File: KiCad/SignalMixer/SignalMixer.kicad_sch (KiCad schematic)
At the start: 33 parts, among them SW1 SW_DIP_x08

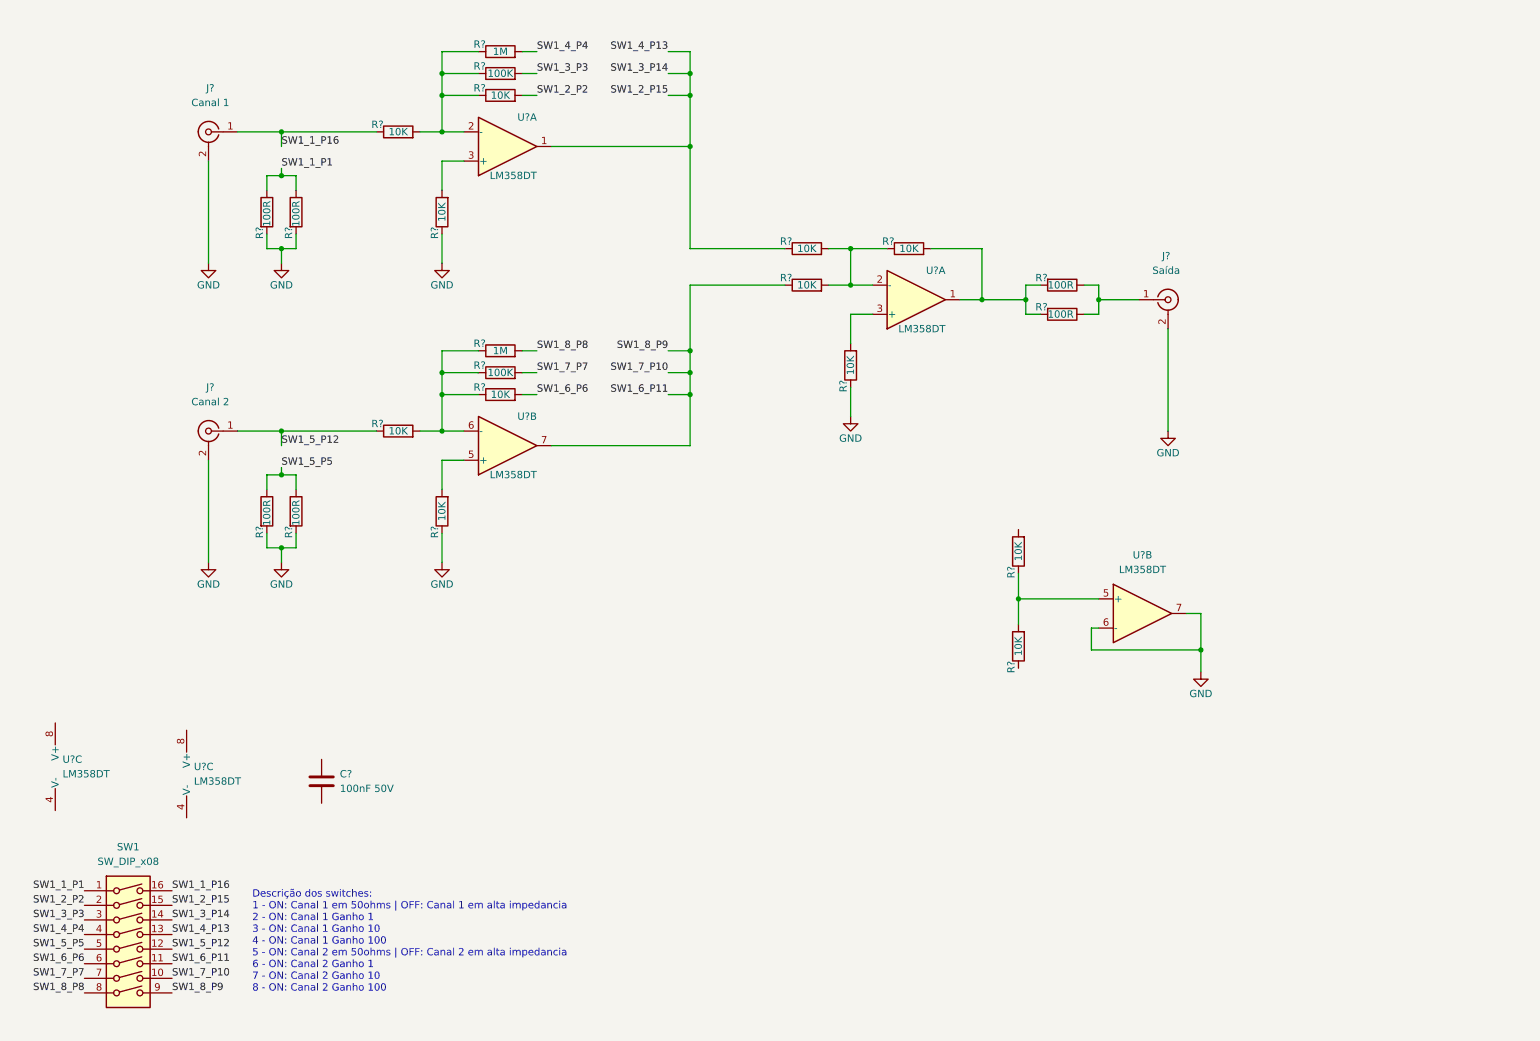
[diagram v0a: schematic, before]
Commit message: Finalização do diagrama esquematico e geração do diagrama em PDF.
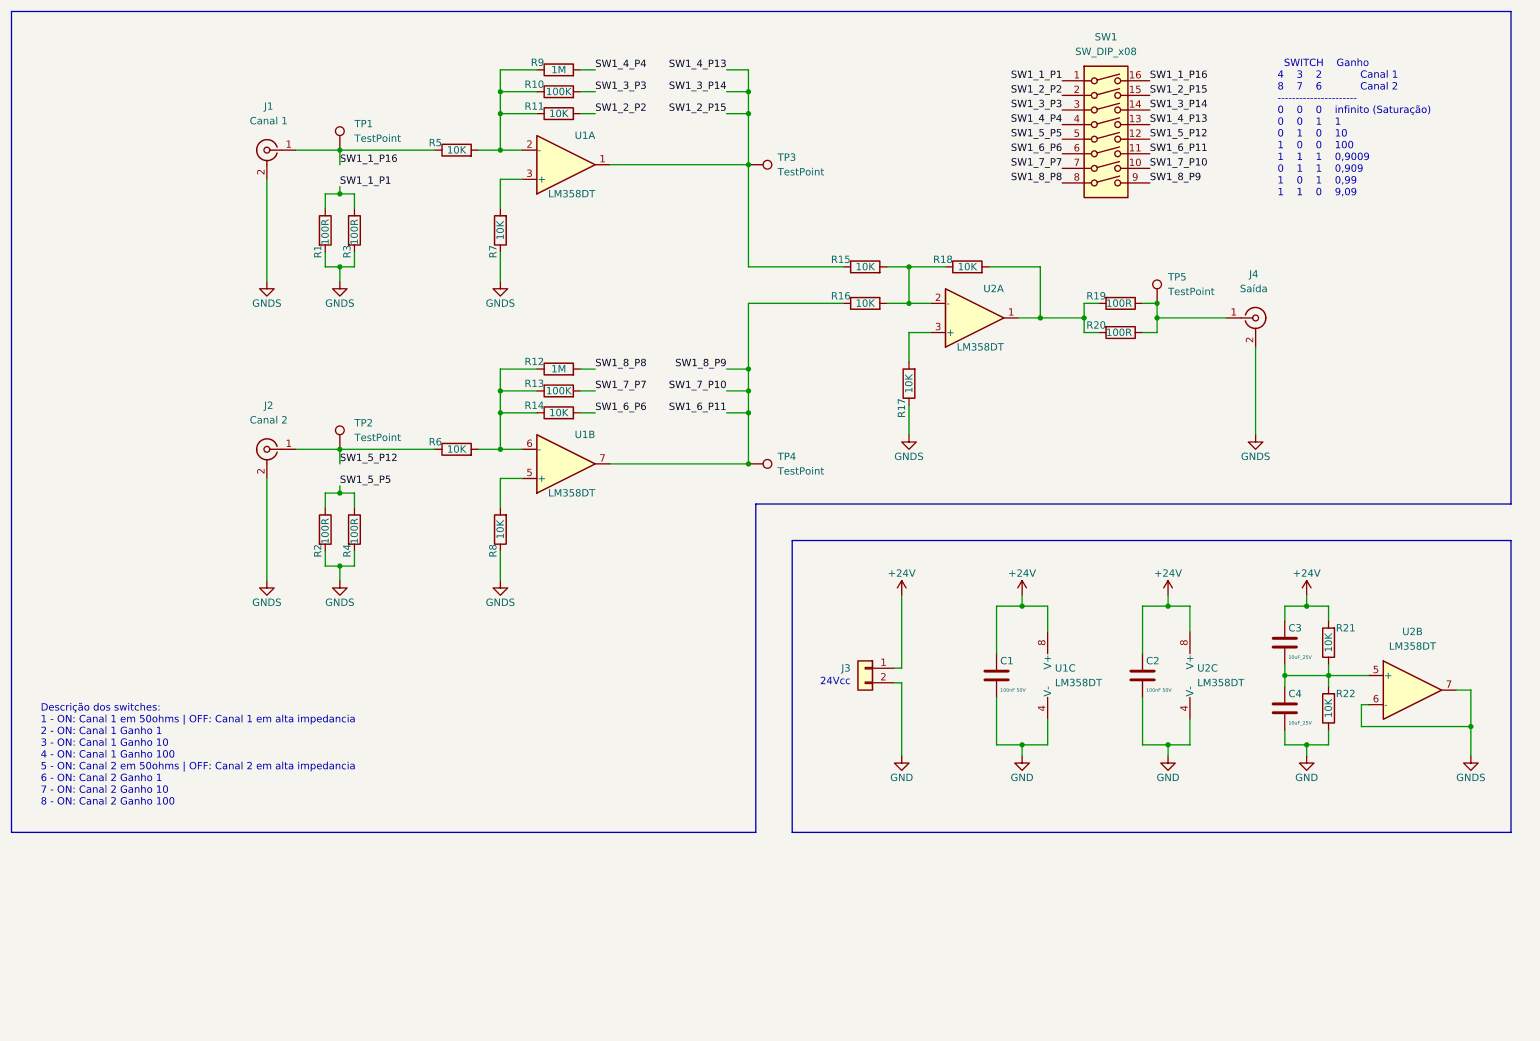
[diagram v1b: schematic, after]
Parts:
- added C1: 100nF 50V, Capacitor_SMD:C_0603_1608Metric, symbol Julio_Capacitores_0603:100nF 50V
- added C3, C4: 10uF_25V, Capacitor_SMD:C_0603_1608Metric, symbol Julio_Capacitores_0603:10uF_25V
- added J3: Conn_01x02, Julio_Connectors:JST_XH_B02B-XH-A_02x2.50mm_Straight, symbol Julio_Conectores:Conn_01x02
- added TP1, TP2, TP3, TP4, TP5: TestPoint, Julio_Testpoints:TestPoint_RH-5000, symbol Julio_Testpoint:TestPoint
- gave numbers to parts that had none: 28
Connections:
- net GND: now also C2.2, R22.1, U1.4 (V-), U2.4 (V-), C1.2, C4.2, J3.2 (Pin_2); no longer J1.2 (Ext), J2.2 (Ext), J4.2 (Ext), R1.2, R17.1, R2.2, R3.2, R4.2, R7.1, R8.1, U2.6 (-), U2.7
- net SW1_1_P16: now also TP1.1
- net SW1_2_P15: now also TP3.1
- net SW1_5_P12: now also TP2.1
- net SW1_6_P11: now also TP4.1
- net at R21.1, R22.2, U2.5 (+): now also C3.2, C4.1
- net +24V: now reaches U1.8 (V+)
- net +24V: now also C2.1, R21.2, U2.8 (V+), C1.1, C3.1, J3.1 (Pin_1)
- net at J4.1 (In), R19.1, R20.1: now also TP5.1
- new net GNDS: J1.2 (Ext), J2.2 (Ext), J4.2 (Ext), R1.2, R17.1, R2.2, R3.2, R4.2, R7.1, R8.1, U2.6 (-), U2.7
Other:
- note added: "24Vcc"
- note added: "SWITCH Ganho 4 3 2 Canal 1 8 7 6 Canal 2 ---------------------- 0 0 0 infinito (Saturação) 0 0 1 1 0 1 0 10 1 0 0 100 1 1 1 0,9009 0 1 1 0,909 1 0 1 0,99 1 1 0 9,09"
- moved on the sheet: C2, J1, J2, J4, R1, R10, R11, R12, R13, R14, R15, R16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

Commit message: Adicionado resistor de 1M nas entradas para evitar flutuacao quando o resistor de 50 ohms for desconectado.
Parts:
- added R1, R2: 1M, Resistor_SMD:R_0603_1608Metric, symbol Julio_Resistores_0603:1M
- added TP6: GNDS, Julio_Testpoints:TestPoint_RH-5000, symbol Julio_Testpoint:TestPoint
- TP1: value TestPoint -> Canal 1
- TP2: value TestPoint -> Canal 2
- TP3: value TestPoint -> Canal_1_G
- TP4: value TestPoint -> Canal_2_G
- TP5: value TestPoint -> Saída
- renumbered R8 to R10, R9 to R11, R10 to R12, R11 to R13, R12 to R14, R13 to R15, R14 to R16, R15 to R17, R16 to R18, R17 to R19, R18 to R20, R19 to R21, R20 to R22, R21 to R23, R22 to R24, R1 to R3, R2 to R4, R3 to R5, R4 to R6, R5 to R7, R6 to R8, R7 to R9
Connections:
- net GNDS: now also R1.1, R2.1, TP6.1
- net SW1_1_P16: now also R1.2
- net SW1_5_P12: now also R2.2
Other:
- moved on the sheet: J1, J2

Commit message: Definicao dos footprints, atualizacao do esquematico e inicio do roteamento da pcb.
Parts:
- J1, J2, J4: footprint (none) -> Julio_Connectors:BNC_DOSIN-801-0083
- SW1: footprint (none) -> Julio_Switches:SW_DIP_SPSTx08_Slide_9.78x22.5mm_W7.62mm_P2.54mm
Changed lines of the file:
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@@
     (property "Reference" "J2" (id 0) (at 59.3724 85.725 0))
     (property "Value" "Canal 2" (id 1) (at 59.3724 88.265 0))
-    (property "Footprint" "" (id 2) (at 59.055 93.345 0)
+    (property "Footprint" "Julio_Connectors:BNC_DOSIN-801-0083" (id 2) (at 59.055 93.345 0)
       (effects (font (size 1.27 1.27)) hide)
     )
@@
     (property "Reference" "J1" (id 0) (at 59.3724 33.655 0))
     (property "Value" "Canal 1" (id 1) (at 59.3724 36.195 0))
-    (property "Footprint" "" (id 2) (at 59.055 41.275 0)
+    (property "Footprint" "Julio_Connectors:BNC_DOSIN-801-0083" (id 2) (at 59.055 41.275 0)
       (effects (font (size 1.27 1.27)) hide)
     )
@@
     (property "Reference" "SW1" (id 0) (at 208.28 21.59 0))
     (property "Value" "SW_DIP_x08" (id 1) (at 208.28 24.13 0))
-    (property "Footprint" "" (id 2) (at 208.28 39.37 0)
+    (property "Footprint" "Julio_Switches:SW_DIP_SPSTx08_Slide_9.78x22.5mm_W7.62mm_P2.54mm" (id 2) (at 208.28 39.37 0)
       (effects (font (size 1.27 1.27)) hide)
     )
@@
     (property "Reference" "J4" (id 0) (at 233.9976 62.865 0))
     (property "Value" "Saída" (id 1) (at 233.9976 65.405 0))
-    (property "Footprint" "" (id 2) (at 234.315 70.485 0)
+    (property "Footprint" "Julio_Connectors:BNC_DOSIN-801-0083" (id 2) (at 234.315 70.485 0)
       (effects (font (size 1.27 1.27)) hide)
     )
@@
     )
     (path "/39b16d0f-89a0-4830-b92f-38d2db5dc07c"
-      (reference "J1") (unit 1) (value "Canal 1") (footprint "")
+      (reference "J1") (unit 1) (value "Canal 1") (footprint "Julio_Connectors:BNC_DOSIN-801-0083")
     )
     (path "/16ce34b0-e124-4278-9fc6-baaedcea88cf"
-      (reference "J2") (unit 1) (value "Canal 2") (footprint "")
+      (reference "J2") (unit 1) (value "Canal 2") (footprint "Julio_Connectors:BNC_DOSIN-801-0083")
     )
     (path "/bc0472ee-2a85-4c9e-9973-2a70e59d9a38"
@@
     )
     (path "/fd9f33df-4147-42df-b32c-afff44c62ea6"
-      (reference "J4") (unit 1) (value "Saída") (footprint "")
+      (reference "J4") (unit 1) (value "Saída") (footprint "Julio_Connectors:BNC_DOSIN-801-0083")
     )
     (path "/8aa91818-5460-4125-a3fc-f6a1805355d8"
@@
     )
     (path "/a2e06167-8355-4f4e-b078-7812a4ea3125"
-      (reference "SW1") (unit 1) (value "SW_DIP_x08") (footprint "")
+      (reference "SW1") (unit 1) (value "SW_DIP_x08") (footprint "Julio_Switches:SW_DIP_SPSTx08_Slide_9.78x22.5mm_W7.62mm_P2.54mm")
     )
     (path "/be7bc791-805c-4e3e-9832-26badc2c2d82"

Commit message: Finalizacao do layout da PCB.
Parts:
- added H1, H2, H3, H4: MountingHole, MountingHole:MountingHole_3.2mm_M3, symbol Mechanical:MountingHole
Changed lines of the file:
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@@
     (pin "2")
+  )
+  (symbol (lib_id "Mechanical:MountingHole") (at 153.035 180.34 0) (unit 1)
+    (in_bom no) (on_board yes) (fields_autoplaced)
+    (property "Reference" "H2" (id 0) (at 156.21 179.0699 0)
+      (effects (font (size 1.27 1.27)) (justify left))
+    )
+    (property "Value" "MountingHole" (id 1) (at 156.21 181.6099 0)
+      (effects (font (size 1.27 1.27)) (justify left))
+    )
+    (property "Footprint" "MountingHole:MountingHole_3.2mm_M3" (id 2) (at 153.035 180.34 0)
+      (effects (font (size 1.27 1.27)) hide)
+    )
+    (property "Datasheet" "~" (id 3) (at 153.035 180.34 0)
+      (effects (font (size 1.27 1.27)) hide)
+    )
   )
   (symbol (lib_id "Julio_Resistores_0603:1M") (at 66.675 107.315 180) (unit 1)
@@
     (pin "1")
     (pin "2")
+  )
+  (symbol (lib_id "Mechanical:MountingHole") (at 153.035 186.055 0) (unit 1)
+    (in_bom no) (on_board yes) (fields_autoplaced)
+    (property "Reference" "H3" (id 0) (at 156.21 184.7849 0)
+      (effects (font (size 1.27 1.27)) (justify left))
+    )
+    (property "Value" "MountingHole" (id 1) (at 156.21 187.3249 0)
+      (effects (font (size 1.27 1.27)) (justify left))
+    )
+    (property "Footprint" "MountingHole:MountingHole_3.2mm_M3" (id 2) (at 153.035 186.055 0)
+      (effects (font (size 1.27 1.27)) hide)
+    )
+    (property "Datasheet" "~" (id 3) (at 153.035 186.055 0)
+      (effects (font (size 1.27 1.27)) hide)
+    )
   )
   (symbol (lib_id "Julio_OpAmp:LM358DT") (at 261.62 135.255 0) (unit 2)
@@
     (pin "2")
   )
+  (symbol (lib_id "Mechanical:MountingHole") (at 153.035 191.77 0) (unit 1)
+    (in_bom no) (on_board yes) (fields_autoplaced)
+    (property "Reference" "H4" (id 0) (at 156.21 190.4999 0)
+      (effects (font (size 1.27 1.27)) (justify left))
+    )
+    (property "Value" "MountingHole" (id 1) (at 156.21 193.0399 0)
+      (effects (font (size 1.27 1.27)) (justify left))
+    )
+    (property "Footprint" "MountingHole:MountingHole_3.2mm_M3" (id 2) (at 153.035 191.77 0)
+      (effects (font (size 1.27 1.27)) hide)
+    )
+    (property "Datasheet" "~" (id 3) (at 153.035 191.77 0)
+      (effects (font (size 1.27 1.27)) hide)
+    )
+  )
   (symbol (lib_id "power:+24V") (at 243.205 118.745 0) (unit 1)
     (in_bom yes) (on_board yes)
@@
     (pin "1")
     (pin "2")
+  )
+  (symbol (lib_id "Mechanical:MountingHole") (at 153.035 174.625 0) (unit 1)
+    (in_bom no) (on_board yes) (fields_autoplaced)
+    (property "Reference" "H1" (id 0) (at 156.21 173.3549 0)
+      (effects (font (size 1.27 1.27)) (justify left))
+    )
+    (property "Value" "MountingHole" (id 1) (at 156.21 175.8949 0)
+      (effects (font (size 1.27 1.27)) (justify left))
+    )
+    (property "Footprint" "MountingHole:MountingHole_3.2mm_M3" (id 2) (at 153.035 174.625 0)
+      (effects (font (size 1.27 1.27)) hide)
+    )
+    (property "Datasheet" "~" (id 3) (at 153.035 174.625 0)
+      (effects (font (size 1.27 1.27)) hide)
+    )
   )
   (symbol (lib_id "Julio_Resistores_0603:100K") (at 113.03 83.185 90) (unit 1)
@@
       (reference "C4") (unit 1) (value "10uF_25V") (footprint "Capacitor_SMD:C_0603_1608Metric")
     )
+    (path "/b565d06f-7fe7-40fa-82ea-44aa2ac9f3bf"
+      (reference "H1") (unit 1) (value "MountingHole") (footprint "MountingHole:MountingHole_3.2mm_M3")
+    )
+    (path "/253ce93a-bf66-48fe-bb4a-777ce79fc1f8"
+      (reference "H2") (unit 1) (value "MountingHole") (footprint "MountingHole:MountingHole_3.2mm_M3")
+    )
+    (path "/31383230-5475-4935-8514-8de3fcade0ee"
+      (reference "H3") (unit 1) (value "MountingHole") (footprint "MountingHole:MountingHole_3.2mm_M3")
+    )
+    (path "/ae89c194-6180-4be5-b7c6-f5c0f1326ed5"
+      (reference "H4") (unit 1) (value "MountingHole") (footprint "MountingHole:MountingHole_3.2mm_M3")
+    )
     (path "/39b16d0f-89a0-4830-b92f-38d2db5dc07c"
